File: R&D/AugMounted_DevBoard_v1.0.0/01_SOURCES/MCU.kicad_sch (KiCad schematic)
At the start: 18 parts, among them J201 J_TYPE-C-31-M-13, U202 U_MCP23017T-E/ML

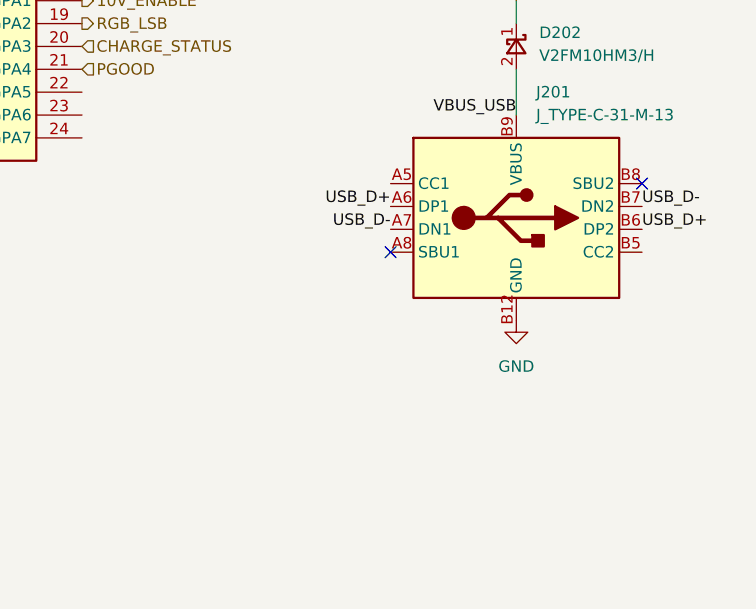
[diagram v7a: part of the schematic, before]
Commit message: Added resistors for CC1 and CC2 pins, layout is started on the high part of the board
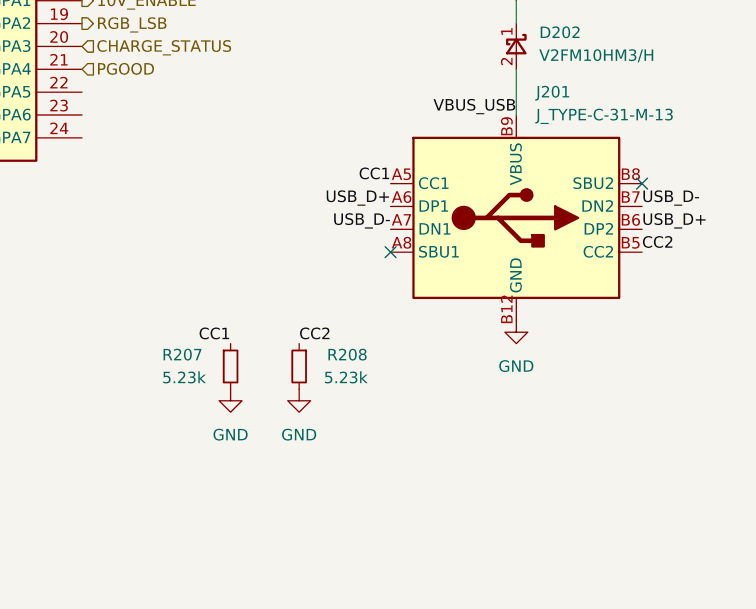
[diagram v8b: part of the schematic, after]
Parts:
- added R207, R208: R_0603_5.23k_1%_0.1W, .mounted-lib:R_0603_1608Metric, symbol .mounted-lib:R_0603_5.23k_1%_0.1W
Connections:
- net CC1: now also J201.A5 (CC1), R207.1
- net CC2: now also J201.B5 (CC2), R208.1
- net GND: now also R207.2, R208.2
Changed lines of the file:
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@@
     (effects (font (size 1.27 1.27)) (justify left bottom))
+  )
+  (label "CC1" (at 228.6 119.38 180) (fields_autoplaced)
+    (effects (font (size 1.27 1.27)) (justify right bottom))
   )
   (label "CC2" (at 273.05 50.8 0) (fields_autoplaced)
     (effects (font (size 1.27 1.27)) (justify left bottom))
   )
+  (label "CC2" (at 274.32 109.22 0) (fields_autoplaced)
+    (effects (font (size 1.27 1.27)) (justify left bottom))
+  )
   (label "USB_D+" (at 247.65 45.72 180) (fields_autoplaced)
     (effects (font (size 1.27 1.27)) (justify right bottom))
@@
     (effects (font (size 1.27 1.27)) (justify right bottom))
   )
+  (label "CC1" (at 246.38 101.6 180) (fields_autoplaced)
+    (effects (font (size 1.27 1.27)) (justify right bottom))
+  )
   (label "USB_D+" (at 274.32 106.68 0) (fields_autoplaced)
     (effects (font (size 1.27 1.27)) (justify left bottom))
@@
   (label "VBUS_USB" (at 260.35 93.98 180) (fields_autoplaced)
     (effects (font (size 1.27 1.27)) (justify right bottom))
+  )
+  (label "CC2" (at 236.22 119.38 0) (fields_autoplaced)
+    (effects (font (size 1.27 1.27)) (justify left bottom))
   )
   (label "RGB_LED_R" (at 171.45 146.05 180) (fields_autoplaced)
@@
     )
   )
+  (symbol (lib_id "power:GND") (at 228.6 124.46 0) (unit 1)
+    (in_bom yes) (on_board yes) (dnp no) (fields_autoplaced)
+    (property "Reference" "#PWR0218" (at 228.6 130.81 0)
+      (effects (font (size 1.27 1.27)) hide)
+    )
+    (property "Value" "GND" (at 228.6 129.54 0)
+      (effects (font (size 1.27 1.27)))
+    )
+    (property "Footprint" "" (at 228.6 124.46 0)
+      (effects (font (size 1.27 1.27)) hide)
+    )
+    (property "Datasheet" "" (at 228.6 124.46 0)
+      (effects (font (size 1.27 1.27)) hide)
+    )
+    (pin "1")
+    (instances
+      (project "AugMounted_DevBoard"
+        (path "/75b08848-9393-425e-a17d-60105119a7b1/a7e357a9-82a1-4b8d-acf0-65ce824c3be5"
+          (reference "#PWR0218") (unit 1)
+        )
+      )
+    )
+  )
   (symbol (lib_id ".mounted-lib:TESTPOINT_1.5MM") (at 39.37 31.75 270) (unit 1)
     (in_bom no) (on_board yes) (dnp no) (fields_autoplaced)
@@
         (path "/75b08848-9393-425e-a17d-60105119a7b1/a7e357a9-82a1-4b8d-acf0-65ce824c3be5"
           (reference "#PWR0203") (unit 1)
+        )
+      )
+    )
+  )
+  (symbol (lib_id ".mounted-lib:R_0603_5.23k_1%_0.1W") (at 228.6 121.92 0) (unit 1)
+    (in_bom yes) (on_board yes) (dnp no)
+    (property "Reference" "R207" (at 220.98 120.65 0)
+      (effects (font (size 1.27 1.27)) (justify left))
+    )
+    (property "Value" "R_0603_5.23k_1%_0.1W" (at 245.11 105.41 0)
+      (effects (font (size 1.27 1.27)) (justify left) hide)
+    )
+    (property "Footprint" ".mounted-lib:R_0603_1608Metric" (at 245.11 122.555 0)
+      (effects (font (size 1.27 1.27)) (justify left) hide)
+    )
+    (property "Datasheet" "http://127.0.0.1" (at 245.11 137.795 0)
+      (effects (font (size 1.27 1.27)) (justify left) hide)
+    )
+    (property "DisplayValue" "5.23k" (at 220.98 123.19 0)
+      (effects (font (size 1.27 1.27)) (justify left))
+    )
+    (property "CMP_ID" "1072" (at 245.11 107.315 0)
+      (effects (font (size 1.27 1.27)) (justify left) hide)
+    )
+    (property "Category" "RESISTOR" (at 245.11 109.22 0)
+      (effects (font (size 1.27 1.27)) (justify left) hide)
+    )
+    (property "Family" "THICK FILM" (at 245.11 111.125 0)
+      (effects (font (size 1.27 1.27)) (justify left) hide)
+    )
+    (property "_Created" "JCN 2023-11-12" (at 245.11 113.03 0)
+      (effects (font (size 1.27 1.27)) (justify left) hide)
+    )
+    (property "_Checked" "" (at 245.11 114.935 0)
+      (effects (font (size 1.27 1.27)) (justify left) hide)
+    )
+    (property "_Confirmed" "" (at 245.11 116.84 0)
+      (effects (font (size 1.27 1.27)) (justify left) hide)
+    )
+    (property "Mount" "SMD" (at 245.11 118.745 0)
+      (effects (font (size 1.27 1.27)) (justify left) hide)
+    )
+    (property "Package" "R0603" (at 245.11 120.65 0)
+      (effects (font (size 1.27 1.27)) (justify left) hide)
+    )
+    (property "PartStatus" "" (at 245.11 122.555 0)
+      (effects (font (size 1.27 1.27)) (justify left) hide)
+    )
+    (property "TempMin_C" "-55°C" (at 245.11 124.46 0)
+      (effects (font (size 1.27 1.27)) (justify left) hide)
+    )
+    (property "TempMax_C" "155°C" (at 245.11 126.365 0)
+      (effects (font (size 1.27 1.27)) (justify left) hide)
+    )
+    (property "Automotive" "Y" (at 245.11 128.27 0)
+      (effects (font (size 1.27 1.27)) (justify left) hide)
+    )
+    (property "MaxHeight_mm" "0.55mm" (at 245.11 130.175 0)
+      (effects (font (size 1.27 1.27)) (justify left) hide)
+    )
+    (property "Tolerance" "1%" (at 245.11 135.89 0)
+      (effects (font (size 1.27 1.27)) (justify left) hide)
+    )
+    (property "Power_W" "0.1W" (at 245.11 132.08 0)
+      (effects (font (size 1.27 1.27)) (justify left) hide)
+    )
+    (pin "1")
+    (pin "2")
+    (instances
+      (project "AugMounted_DevBoard"
+        (path "/75b08848-9393-425e-a17d-60105119a7b1/a7e357a9-82a1-4b8d-acf0-65ce824c3be5"
+          (reference "R207") (unit 1)
         )
       )
@@
         (path "/75b08848-9393-425e-a17d-60105119a7b1/a7e357a9-82a1-4b8d-acf0-65ce824c3be5"
           (reference "R204") (unit 1)
+        )
+      )
+    )
+  )
+  (symbol (lib_id "power:GND") (at 236.22 124.46 0) (unit 1)
+    (in_bom yes) (on_board yes) (dnp no) (fields_autoplaced)
+    (property "Reference" "#PWR0217" (at 236.22 130.81 0)
+      (effects (font (size 1.27 1.27)) hide)
+    )
+    (property "Value" "GND" (at 236.22 129.54 0)
+      (effects (font (size 1.27 1.27)))
+    )
+    (property "Footprint" "" (at 236.22 124.46 0)
+      (effects (font (size 1.27 1.27)) hide)
+    )
+    (property "Datasheet" "" (at 236.22 124.46 0)
+      (effects (font (size 1.27 1.27)) hide)
+    )
+    (pin "1")
+    (instances
+      (project "AugMounted_DevBoard"
+        (path "/75b08848-9393-425e-a17d-60105119a7b1/a7e357a9-82a1-4b8d-acf0-65ce824c3be5"
+          (reference "#PWR0217") (unit 1)
         )
       )
@@
         )
       )
+    )
+  )
+  (symbol (lib_id ".mounted-lib:R_0603_5.23k_1%_0.1W") (at 236.22 121.92 0) (mirror y) (unit 1)
+    (in_bom yes) (on_board yes) (dnp no)
+    (property "Reference" "R208" (at 243.84 120.65 0)
+      (effects (font (size 1.27 1.27)) (justify left))
+    )
+    (property "Value" "R_0603_5.23k_1%_0.1W" (at 219.71 105.41 0)
+      (effects (font (size 1.27 1.27)) (justify left) hide)
+    )
+    (property "Footprint" ".mounted-lib:R_0603_1608Metric" (at 219.71 122.555 0)
+      (effects (font (size 1.27 1.27)) (justify left) hide)
+    )
+    (property "Datasheet" "http://127.0.0.1" (at 219.71 137.795 0)
+      (effects (font (size 1.27 1.27)) (justify left) hide)
+    )
+    (property "DisplayValue" "5.23k" (at 243.84 123.19 0)
+      (effects (font (size 1.27 1.27)) (justify left))
+    )
+    (property "CMP_ID" "1072" (at 219.71 107.315 0)
+      (effects (font (size 1.27 1.27)) (justify left) hide)
+    )
+    (property "Category" "RESISTOR" (at 219.71 109.22 0)
+      (effects (font (size 1.27 1.27)) (justify left) hide)
+    )
+    (property "Family" "THICK FILM" (at 219.71 111.125 0)
+      (effects (font (size 1.27 1.27)) (justify left) hide)
+    )
+    (property "_Created" "JCN 2023-11-12" (at 219.71 113.03 0)
+      (effects (font (size 1.27 1.27)) (justify left) hide)
+    )
+    (property "_Checked" "" (at 219.71 114.935 0)
+      (effects (font (size 1.27 1.27)) (justify left) hide)
+    )
+    (property "_Confirmed" "" (at 219.71 116.84 0)
+      (effects (font (size 1.27 1.27)) (justify left) hide)
+    )
+    (property "Mount" "SMD" (at 219.71 118.745 0)
+      (effects (font (size 1.27 1.27)) (justify left) hide)
+    )
+    (property "Package" "R0603" (at 219.71 120.65 0)
+      (effects (font (size 1.27 1.27)) (justify left) hide)
+    )
+    (property "PartStatus" "" (at 219.71 122.555 0)
+      (effects (font (size 1.27 1.27)) (justify left) hide)
+    )
+    (property "TempMin_C" "-55°C" (at 219.71 124.46 0)
+      (effects (font (size 1.27 1.27)) (justify left) hide)
+    )
+    (property "TempMax_C" "155°C" (at 219.71 126.365 0)
+      (effects (font (size 1.27 1.27)) (justify left) hide)
+    )
+    (property "Automotive" "Y" (at 219.71 128.27 0)
+      (effects (font (size 1.27 1.27)) (justify left) hide)
+    )
+    (property "MaxHeight_mm" "0.55mm" (at 219.71 130.175 0)
+      (effects (font (size 1.27 1.27)) (justify left) hide)
+    )
+    (property "Tolerance" "1%" (at 219.71 135.89 0)
+      (effects (font (size 1.27 1.27)) (justify left) hide)
+    )
+    (property "Power_W" "0.1W" (at 219.71 132.08 0)
+      (effects (font (size 1.27 1.27)) (justify left) hide)
+    )
+    (pin "1")
+    (pin "2")
+    (instances
+      (project "AugMounted_DevBoard"
+        (path "/75b08848-9393-425e-a17d-60105119a7b1/a7e357a9-82a1-4b8d-acf0-65ce824c3be5"
+          (reference "R208") (unit 1)
+        )
+      )
